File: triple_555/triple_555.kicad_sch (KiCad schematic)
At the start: 24 parts, among them J1 Conn_01x04, J2 Conn_01x04, U1 NA555P, U2 NA555P, U3 NA555P

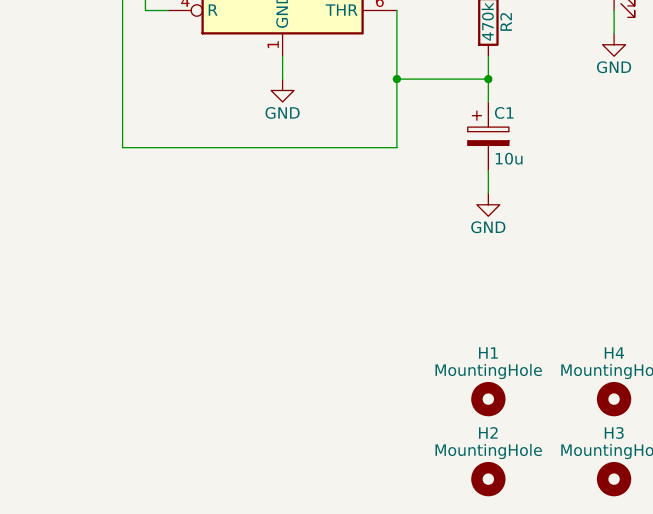
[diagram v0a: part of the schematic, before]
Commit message: add alt value table
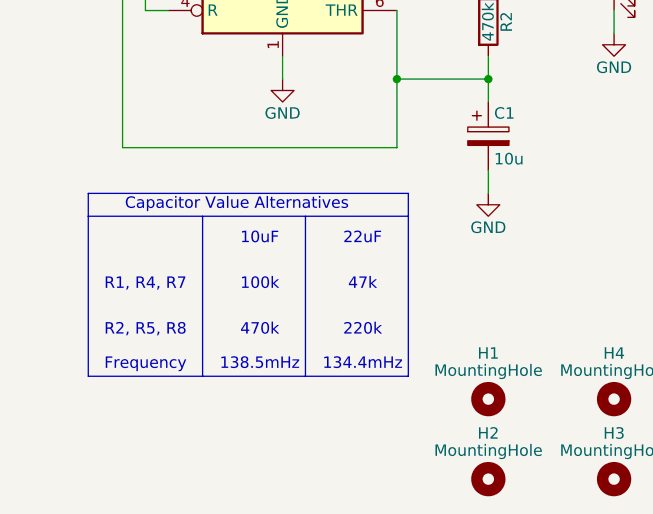
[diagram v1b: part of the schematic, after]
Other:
- note added: "100k"
- note added: "10uF"
- note added: "134.4mHz"
- note added: "138.5mHz"
- note added: "220k"
- note added: "22uF"
- note added: "470k"
- note added: "47k"
- note added: "Capacitor Value Alternatives"
- note added: "Frequency"
- note added: "R1, R4, R7"
- note added: "R2, R5, R8"
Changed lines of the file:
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@@
+		)
+	)
+	(polyline
+		(pts
+			(xy 59.69 113.03) (xy 59.69 130.81)
+		)
+		(stroke
+			(width 0)
+			(type default)
 		)
 	)
@@
 		)
 	)
+	(polyline
+		(pts
+			(xy 46.99 113.03) (xy 46.99 110.49)
+		)
+		(stroke
+			(width 0)
+			(type default)
+		)
+	)
 	(wire
 		(pts
@@
 		)
 	)
+	(polyline
+		(pts
+			(xy 82.55 110.49) (xy 82.55 113.03)
+		)
+		(stroke
+			(width 0)
+			(type default)
+		)
+	)
 	(wire
 		(pts
@@
 		)
 	)
+	(polyline
+		(pts
+			(xy 46.99 110.49) (xy 82.55 110.49)
+		)
+		(stroke
+			(width 0)
+			(type default)
+		)
+	)
 	(wire
 		(pts
@@
 		)
 	)
+	(polyline
+		(pts
+			(xy 71.12 113.03) (xy 71.12 130.81)
+		)
+		(stroke
+			(width 0)
+			(type default)
+		)
+	)
 	(wire
 		(pts
@@
 		)
 	)
+	(rectangle
+		(start 46.99 113.03)
+		(end 82.55 130.81)
+		(stroke
+			(width 0)
+			(type default)
+		)
+		(fill
+			(type none)
+		)
+	)
+	(text "138.5mHz"
+		(exclude_from_sim no)
+		(at 66.04 129.54 0)
+		(effects
+			(font
+				(size 1.27 1.27)
+			)
+		)
+	)
+	(text "R2, R5, R8"
+		(exclude_from_sim no)
+		(at 53.34 125.73 0)
+		(effects
+			(font
+				(size 1.27 1.27)
+			)
+		)
+	)
+	(text "Capacitor Value Alternatives"
+		(exclude_from_sim no)
+		(at 63.5 111.76 0)
+		(effects
+			(font
+				(size 1.27 1.27)
+			)
+		)
+	)
+	(text "Frequency"
+		(exclude_from_sim no)
+		(at 53.34 129.54 0)
+		(effects
+			(font
+				(size 1.27 1.27)
+			)
+		)
+	)
+	(text "220k"
+		(exclude_from_sim no)
+		(at 77.47 125.73 0)
+		(effects
+			(font
+				(size 1.27 1.27)
+			)
+		)
+	)
+	(text "47k"
+		(exclude_from_sim no)
+		(at 77.47 120.65 0)
+		(effects
+			(font
+				(size 1.27 1.27)
+			)
+		)
+	)
+	(text "22uF"
+		(exclude_from_sim no)
+		(at 77.47 115.57 0)
+		(effects
+			(font
+				(size 1.27 1.27)
+			)
+		)
+	)
+	(text "134.4mHz"
+		(exclude_from_sim no)
+		(at 77.47 129.54 0)
+		(effects
+			(font
+				(size 1.27 1.27)
+			)
+		)
+	)
+	(text "10uF"
+		(exclude_from_sim no)
+		(at 66.04 115.57 0)
+		(effects
+			(font
+				(size 1.27 1.27)
+			)
+		)
+	)
+	(text "100k"
+		(exclude_from_sim no)
+		(at 66.04 120.65 0)
+		(effects
+			(font
+				(size 1.27 1.27)
+			)
+		)
+	)
+	(text "470k"
+		(exclude_from_sim no)
+		(at 66.04 125.73 0)
+		(effects
+			(font
+				(size 1.27 1.27)
+			)
+		)
+	)
+	(text "R1, R4, R7"
+		(exclude_from_sim no)
+		(at 53.34 120.65 0)
+		(effects
+			(font
+				(size 1.27 1.27)
+			)
+		)
+	)

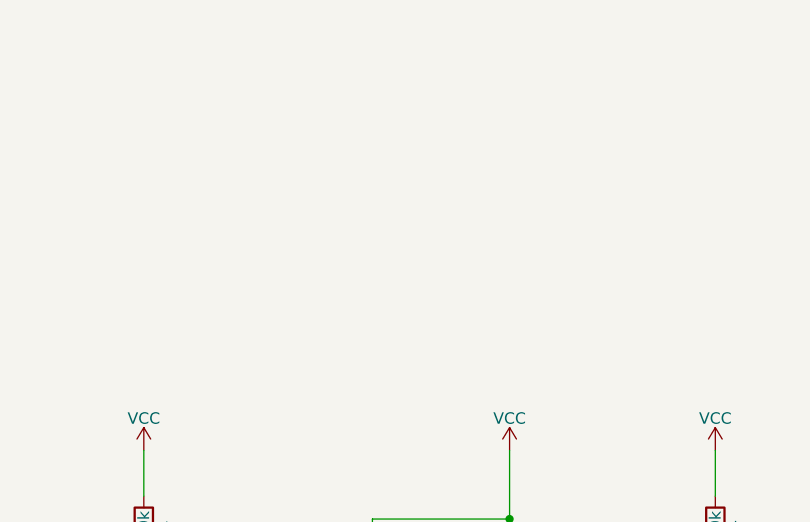
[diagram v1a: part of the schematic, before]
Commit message: add usb b connector
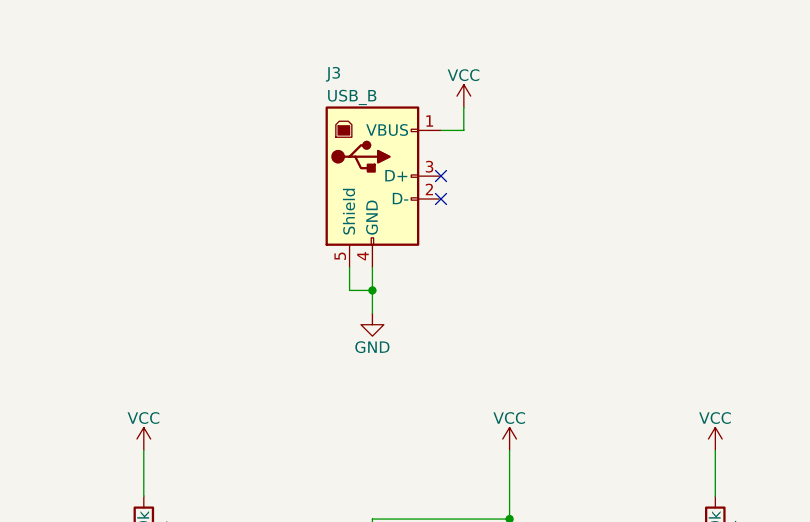
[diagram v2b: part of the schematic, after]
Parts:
- added J3: USB_B, pl_usb:USB_B_mill_spacing, symbol Connector:USB_B
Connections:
- net GND: now also J3.4 (GND), J3.5 (Shield)
- net VCC: now also J3.1 (VBUS)
- no-connect marks 3 -> 5

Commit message: set title
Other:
- title: Battery Leakage Generator - 3x 555 -> Tripple 555
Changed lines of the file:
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@@
 	(paper "A")
 	(title_block
-		(title "Battery Leakage Generator - 3x 555")
+		(title "Tripple 555")
 		(date "2024-11-22")
 		(company "Perry Leumas")

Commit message: resize table
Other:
- note added: "C1, C2, C3"
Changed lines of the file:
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@@
 	(title_block
 		(title "Tripple 555")
-		(date "2024-11-22")
+		(date "2024-11-24")
+		(rev "A")
 		(company "Perry Leumas")
 		(comment 1 "Source: https://www.youtube.com/watch?v=Gr6gBjDxP5M&t=176s")
@@
 	(polyline
 		(pts
-			(xy 59.69 113.03) (xy 59.69 130.81)
+			(xy 59.69 113.03) (xy 59.69 124.46)
 		)
 		(stroke
@@
 	(polyline
 		(pts
-			(xy 71.12 113.03) (xy 71.12 130.81)
+			(xy 71.12 113.03) (xy 71.12 124.46)
 		)
 		(stroke
@@
 	(rectangle
 		(start 46.99 113.03)
-		(end 82.55 130.81)
+		(end 82.55 124.46)
 		(stroke
 			(width 0)
@@
 		)
 	)
-	(text "138.5mHz"
-		(exclude_from_sim no)
-		(at 66.04 129.54 0)
+	(text "C1, C2, C3"
+		(exclude_from_sim no)
+		(at 53.34 115.57 0)
 		(effects
 			(font
@@
 		)
 	)
-	(text "R2, R5, R8"
-		(exclude_from_sim no)
-		(at 53.34 125.73 0)
+	(text "138.5mHz"
+		(exclude_from_sim no)
+		(at 66.04 123.19 0)
 		(effects
 			(font
@@
 		)
 	)
-	(text "Capacitor Value Alternatives"
-		(exclude_from_sim no)
-		(at 63.5 111.76 0)
+	(text "R2, R5, R8"
+		(exclude_from_sim no)
+		(at 53.34 120.65 0)
 		(effects
 			(font
@@
 		)
 	)
-	(text "Frequency"
-		(exclude_from_sim no)
-		(at 53.34 129.54 0)
+	(text "Capacitor Value Alternatives"
+		(exclude_from_sim no)
+		(at 63.5 111.76 0)
 		(effects
 			(font
@@
 		)
 	)
-	(text "220k"
-		(exclude_from_sim no)
-		(at 77.47 125.73 0)
+	(text "Frequency"
+		(exclude_from_sim no)
+		(at 53.34 123.19 0)
 		(effects
 			(font
@@
 		)
 	)
-	(text "47k"
+	(text "220k"
 		(exclude_from_sim no)
 		(at 77.47 120.65 0)
@@
 		)
 	)
-	(text "22uF"
-		(exclude_from_sim no)
-		(at 77.47 115.57 0)
+	(text "47k"
+		(exclude_from_sim no)
+		(at 77.47 118.11 0)
 		(effects
 			(font
@@
 		)
 	)
-	(text "134.4mHz"
-		(exclude_from_sim no)
-		(at 77.47 129.54 0)
+	(text "22uF"
+		(exclude_from_sim no)
+		(at 77.47 115.57 0)
 		(effects
 			(font
@@
 		)
 	)
-	(text "10uF"
-		(exclude_from_sim no)
-		(at 66.04 115.57 0)
+	(text "134.4mHz"
+		(exclude_from_sim no)
+		(at 77.47 123.19 0)
 		(effects
 			(font
@@
 		)
 	)
-	(text "100k"
-		(exclude_from_sim no)
-		(at 66.04 120.65 0)
+	(text "10uF"
+		(exclude_from_sim no)
+		(at 66.04 115.57 0)
 		(effects
 			(font
@@
 		)
 	)
-	(text "470k"
-		(exclude_from_sim no)
-		(at 66.04 125.73 0)
+	(text "100k"
+		(exclude_from_sim no)
+		(at 66.04 118.11 0)
 		(effects
 			(font
@@
 		)
 	)
+	(text "470k"
+		(exclude_from_sim no)
+		(at 66.04 120.65 0)
+		(effects
+			(font
+				(size 1.27 1.27)
+			)
+		)
+	)
 	(text "R1, R4, R7"
 		(exclude_from_sim no)
-		(at 53.34 120.65 0)
-		(effects
-			(font
+		(at 53.34 118.11 0)
+		(effects
+			(font
